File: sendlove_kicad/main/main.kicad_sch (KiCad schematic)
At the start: 50 parts, among them J1 USB-C 16P, J2 BATT, J3 LCD_ST7789_240x240, J4 microSD DM3AT, J5 SPEAKER 8R 1W, Q1 AO3401A, SW1 POWER, SW2 RESET, SW3 BOOT, U1 USBLC6-2SC6, U2 TP4056-42-ESOP8, U3 RT9080-33GJ5, U4 ESP32-C3-MINI-1-N4, U5 MAX98357AETE+, U6 TTP223-BA6

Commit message: fix(hw): RT9080 dung footprint TSOT-23-5, ghi ket qua doi chieu datasheet
- RT9080-33GJ5 la goi TSOT-23-5 (datasheet DS9080-09), doi footprint tu SOT-23-5.
  So do chan 1 VIN, 2 GND, 3 EN, 4 NC, 5 VOUT khop symbol da tao.
- TP4056-42: nguong TEMP 45%/80% VIN da doi chieu datasheet rev 2.4. Voi NTC
  B3950 + 6.2k, cua so sac thuc te ~6-41 do C (truoc ghi ~5-45).
- Da doi 15 cap GPIO <-> nhan net cua U4 voi bang chan BOM.md: khop het.

Co-Authored-By: Claude Opus 5.5 <noreply@anthropic.com>
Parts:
- U3: footprint Package_TO_SOT_SMD:SOT-23-5 -> Package_TO_SOT_SMD:TSOT-23-5
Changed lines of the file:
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@@
 			)
 		)
-		(property "Footprint" "Package_TO_SOT_SMD:SOT-23-5"
+		(property "Footprint" "Package_TO_SOT_SMD:TSOT-23-5"
 			(at 142.24 124.46 0)
 			(hide yes)

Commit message: refactor(hw): ve lai schematic - khoi USB-C + ESD (dang lam, chua du khoi)
Bat dau ve lai trinh bay toan bo schematic: linh kien phu sat IC, noi bang day,
GND/+3V3/VBUS dung ky hieu nguon, nhan chi cho tin hieu giua cac khoi. Ket noi
giu nguyen, doi chieu voi netlist cu (b7ea78a) khi xong. Ban day du cuoi cung
truoc khi ve lai: b7ea78a.

Co-Authored-By: Claude Opus 5.5 <noreply@anthropic.com>
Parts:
- removed C1, C10, C2, C3, C4: 10uF, Capacitor_SMD:C_0805_2012Metric, symbol Device:C
- removed C11, C13, C6, C9: 100nF, Capacitor_SMD:C_0402_1005Metric, symbol Device:C
- removed C12: 10pF (0-50pF), Capacitor_SMD:C_0603_1608Metric, symbol Device:C
- removed C5, C8: 10uF, Capacitor_SMD:C_0603_1608Metric, symbol Device:C
- removed C7: 1uF, Capacitor_SMD:C_0603_1608Metric, symbol Device:C
- removed D1: SS14, Diode_SMD:D_SMA, symbol Device:D_Schottky
- removed D2: LED_Red, LED_SMD:LED_0603_1608Metric, symbol Device:LED
- removed D3: LED_NOTIFY, LED_SMD:LED_0603_1608Metric, symbol Device:LED
- removed J2: BATT, Connector_JST:JST_PH_S2B-PH-SM4-TB_1x02-1MP_P2.00mm_Horizontal, symbol Connector_Generic:Conn_01x02
- removed J3: LCD_ST7789_240x240, Connector_PinHeader_2.54mm:PinHeader_1x07_P2.54mm_Vertical, symbol Connector_Generic:Conn_01x07
- removed J4: microSD DM3AT, Connector_Card:microSD_HC_Hirose_DM3AT-SF-PEJM5, symbol Connector:Micro_SD_Card_Det_Hirose_DM3AT
- removed J5: SPEAKER 8R 1W, Connector_JST:JST_PH_S2B-PH-SM4-TB_1x02-1MP_P2.00mm_Horizontal, symbol Connector_Generic:Conn_01x02
- removed Q1: AO3401A, Package_TO_SOT_SMD:SOT-23, symbol Transistor_FET:AO3401A
- removed R10, R11, R12, R13, R14, R15, R7, R9: 10k, Resistor_SMD:R_0603_1608Metric, symbol Device:R
- removed R16: 680k, Resistor_SMD:R_0603_1608Metric, symbol Device:R
- removed R17, R5, R8: 1k, Resistor_SMD:R_0603_1608Metric, symbol Device:R
- removed R3: 2k, Resistor_SMD:R_0603_1608Metric, symbol Device:R
- removed R4: 6.2k 1%, Resistor_SMD:R_0603_1608Metric, symbol Device:R
- removed R6: 100k, Resistor_SMD:R_0603_1608Metric, symbol Device:R
- removed SW1: POWER, Button_Switch_SMD:SW_SPDT_PCM12, symbol Switch:SW_SPDT
- removed SW2: RESET, Button_Switch_SMD:SW_SPST_PTS810, symbol Switch:SW_Push
- removed SW3: BOOT, Button_Switch_SMD:SW_SPST_PTS810, symbol Switch:SW_Push
- removed TH1: 10k B3950, Resistor_SMD:R_0603_1608Metric, symbol Device:Thermistor_NTC
- removed TP1: TOUCH_PAD, TestPoint:TestPoint_Pad_D4.0mm, symbol Connector:TestPoint
- removed U2: TP4056-42-ESOP8, Package_SO:SOIC-8-1EP_3.9x4.9mm_P1.27mm_EP2.41x3.3mm_ThermalVias, symbol Battery_Management:TP4056-42-ESOP8
- removed U3: RT9080-33GJ5, Package_TO_SOT_SMD:TSOT-23-5, symbol SendLove:RT9080-33GJ5
- removed U4: ESP32-C3-MINI-1-N4, PCM_Espressif:ESP32-C3-MINI-1, symbol Espressif:ESP32-C3-MINI-1
- removed U5: MAX98357AETE+, Package_DFN_QFN:TQFN-16-1EP_3x3mm_P0.5mm_EP1.23x1.23mm, symbol Audio:MAX98357A
- removed U6: TTP223-BA6, Package_TO_SOT_SMD:SOT-23-6, symbol SendLove:TTP223-BA6
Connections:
- net USB_DN: no longer J1.A7 (D-), J1.B7 (D-), U1.1 (I/O1)
- net USB_DP: no longer J1.A6 (D+), J1.B6 (D+), U1.3 (I/O2)
- net CC1: no longer names the net of J1.A5 (CC1), R1.1
- net CC2: no longer names the net of J1.B5 (CC2), R2.1
- new net: J1.A7 (D-), J1.B7 (D-), U1.1 (I/O1)
- new net: J1.A6 (D+), J1.B6 (D+), U1.3 (I/O2)
- no-connect marks 7 -> 2
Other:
- note added: "1. USB-C + ESD"

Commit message: refactor(hw): ve lai schematic - khoi sac TP4056 (dang lam)
Co-Authored-By: Claude Opus 5.5 <noreply@anthropic.com>
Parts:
- added C1, C2: 10uF, Capacitor_SMD:C_0805_2012Metric, symbol Device:C
- added D2: LED_Red, LED_SMD:LED_0603_1608Metric, symbol Device:LED
- added R3: 2k, Resistor_SMD:R_0603_1608Metric, symbol Device:R
- added R4: 6.2k 1%, Resistor_SMD:R_0603_1608Metric, symbol Device:R
- added R5: 1k, Resistor_SMD:R_0603_1608Metric, symbol Device:R
- added TH1: 10k B3950, Resistor_SMD:R_0603_1608Metric, symbol Device:Thermistor_NTC
- added U2: TP4056-42-ESOP8, Package_SO:SOIC-8-1EP_3.9x4.9mm_P1.27mm_EP2.41x3.3mm_ThermalVias, symbol Battery_Management:TP4056-42-ESOP8
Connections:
- net GND: now also C1.2, C2.2, R3.2, TH1.2, U2.3 (GND), U2.9 (EPAD)
- net VBUS: now also C1.1, D2.2 (A), R4.1, U2.4 (V_{CC}), U2.8 (CE)
- new net: D2.1 (K), R5.1
- new net: R4.2, TH1.1, U2.1 (TEMP)
- new net: R3.1, U2.2 (PROG)
- new net: R5.2, U2.7 (~{CHRG})
- new net VBAT: C2.1, U2.5 (BAT)
- no-connect marks 2 -> 3
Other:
- note added: "2. Sac pin TP4056 (~580mA, NTC 6-41 do C)"

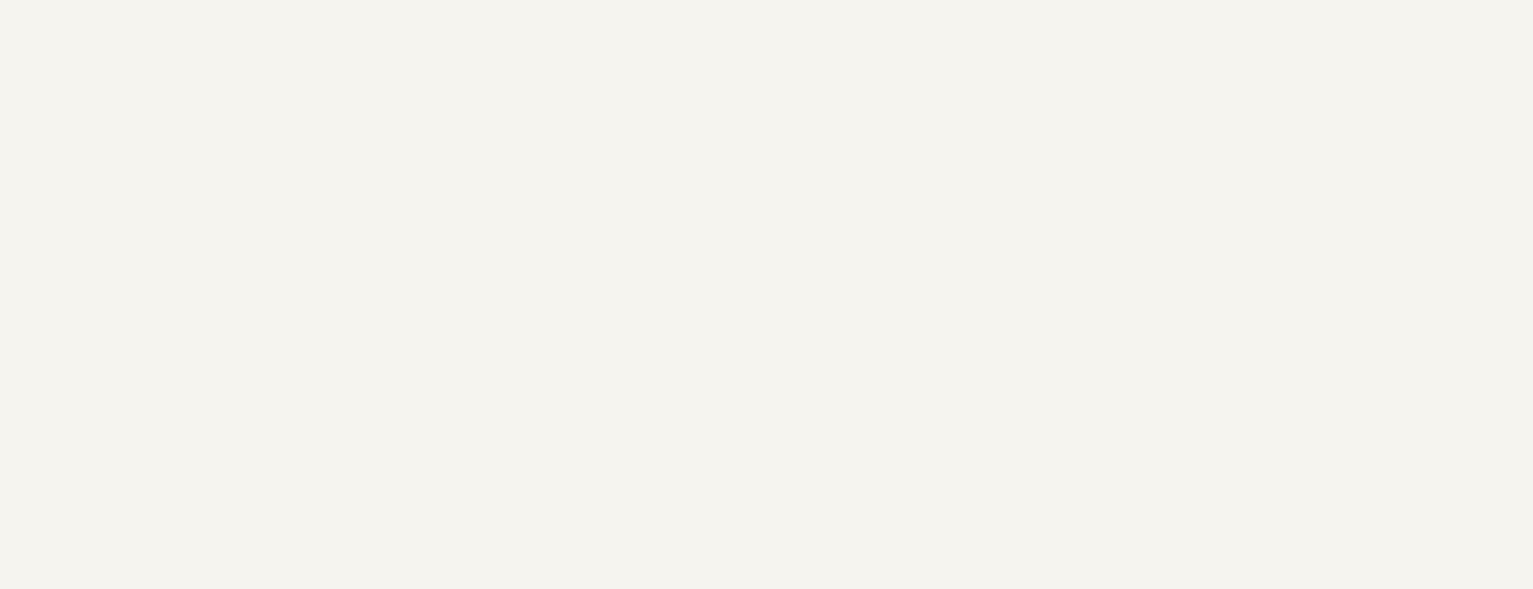
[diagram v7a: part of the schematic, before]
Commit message: refactor(hw): ve lai schematic - khoi chon nguon + LDO (dang lam)
Co-Authored-By: Claude Opus 5.5 <noreply@anthropic.com>
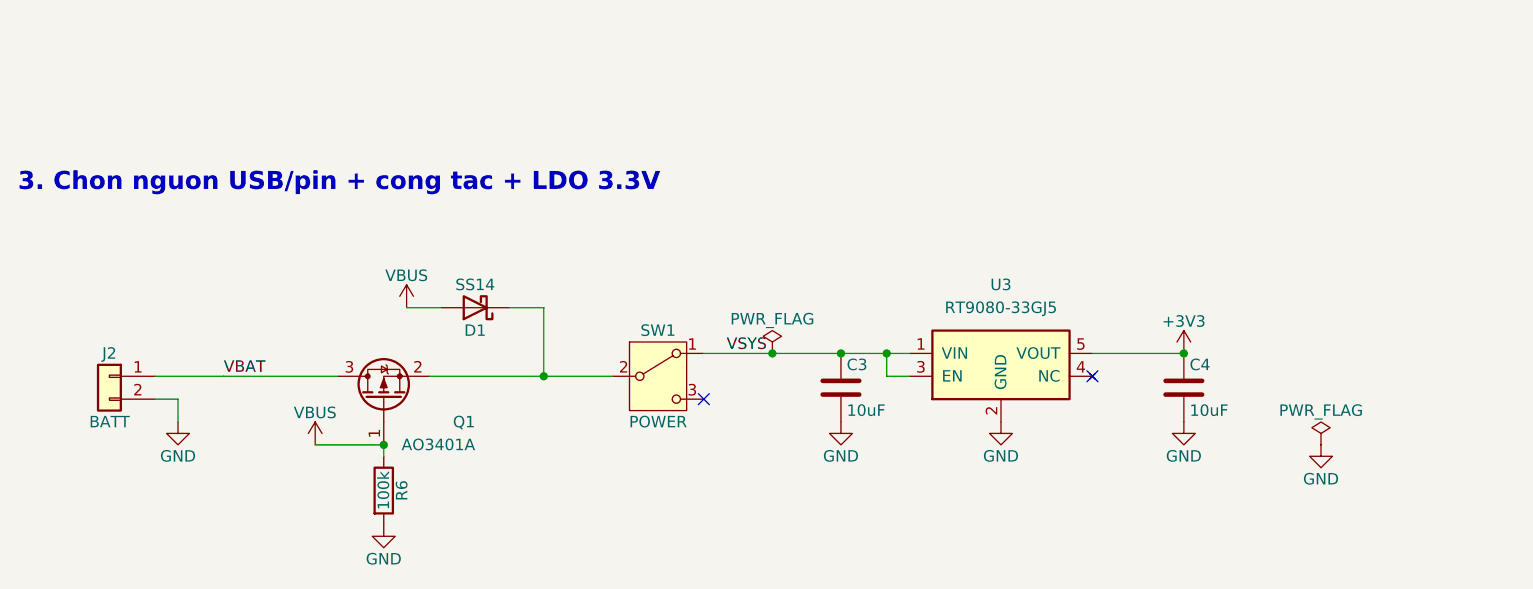
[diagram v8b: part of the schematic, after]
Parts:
- added C3, C4: 10uF, Capacitor_SMD:C_0805_2012Metric, symbol Device:C
- added D1: SS14, Diode_SMD:D_SMA, symbol Device:D_Schottky
- added J2: BATT, Connector_JST:JST_PH_S2B-PH-SM4-TB_1x02-1MP_P2.00mm_Horizontal, symbol Connector_Generic:Conn_01x02
- added Q1: AO3401A, Package_TO_SOT_SMD:SOT-23, symbol Transistor_FET:AO3401A
- added R6: 100k, Resistor_SMD:R_0603_1608Metric, symbol Device:R
- added SW1: POWER, Button_Switch_SMD:SW_SPDT_PCM12, symbol Switch:SW_SPDT
- added U3: RT9080-33GJ5, Package_TO_SOT_SMD:TSOT-23-5, symbol SendLove:RT9080-33GJ5
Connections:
- net GND: now also C3.2, C4.2, J2.2 (Pin_2), R6.2, U3.2 (GND)
- net VBAT: now also J2.1 (Pin_1), Q1.3 (D)
- net VBUS: now also D1.2 (A), Q1.1 (G), R6.1
- new net: D1.1 (K), Q1.2 (S), SW1.2 (B)
- new net +3V3: C4.1, U3.5 (VOUT)
- new net VSYS: C3.1, SW1.1 (A), U3.1 (VIN), U3.3 (EN)
- no-connect marks 3 -> 5
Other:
- note added: "3. Chon nguon USB/pin + cong tac + LDO 3.3V"
